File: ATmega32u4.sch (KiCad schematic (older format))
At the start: 36 parts, among them J1 USB_B_Mini, U4 ATmega32U4RC-MU, Y1 16MHz

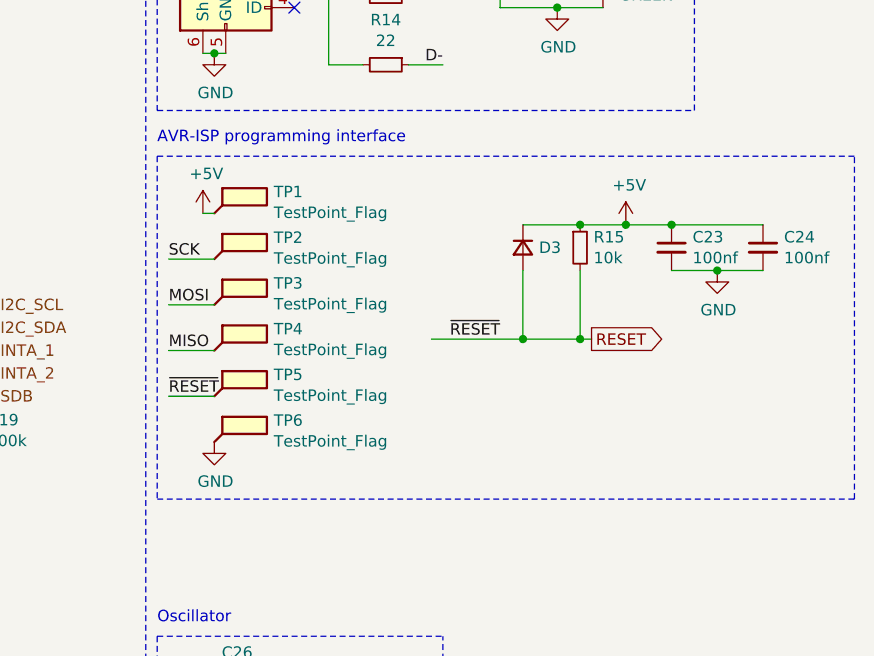
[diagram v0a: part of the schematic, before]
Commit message: Switch to jtag
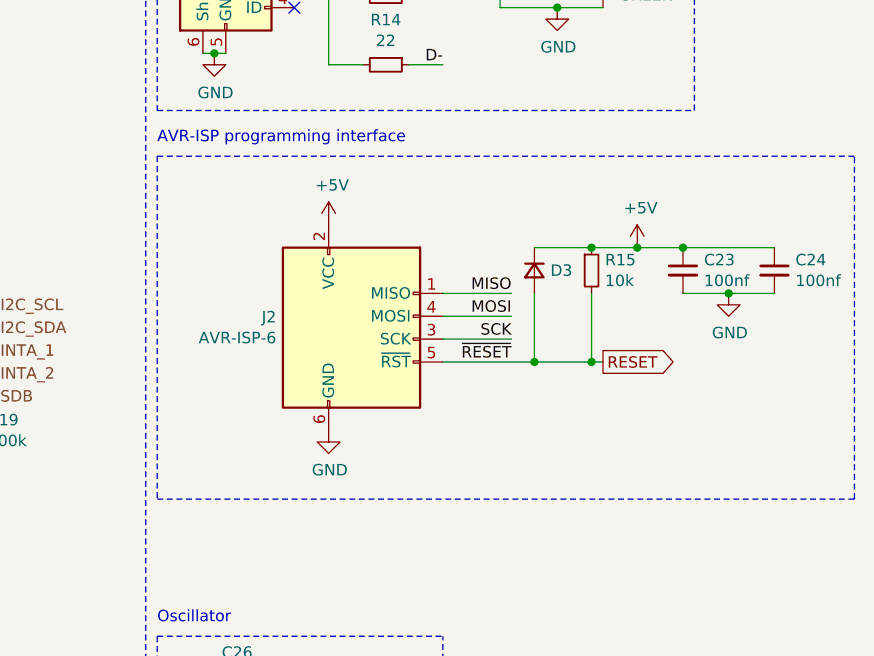
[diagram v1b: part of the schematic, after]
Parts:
- removed TP1, TP2, TP3, TP4, TP5, TP6: TestPoint_Flag, TestPoint:TestPoint_THTPad_D1.0mm_Drill0.5mm, symbol Connector:TestPoint_Flag
- added J2: AVR-ISP-6, Connector:Tag-Connect_TC2030-IDC-NL_2x03_P1.27mm_Vertical, symbol Connector:AVR-ISP-6
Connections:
- net +5V: now also J2.2 (VCC)
- net GND: now also J2.6 (GND)
- net MISO: now also J2.1 (MISO)
- net MOSI: now also J2.4 (MOSI)
- net RESET: now also J2.5 (~RST)
- net SCK: now also J2.3 (SCK)
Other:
- moved on the sheet: C23, C24, D3, R15

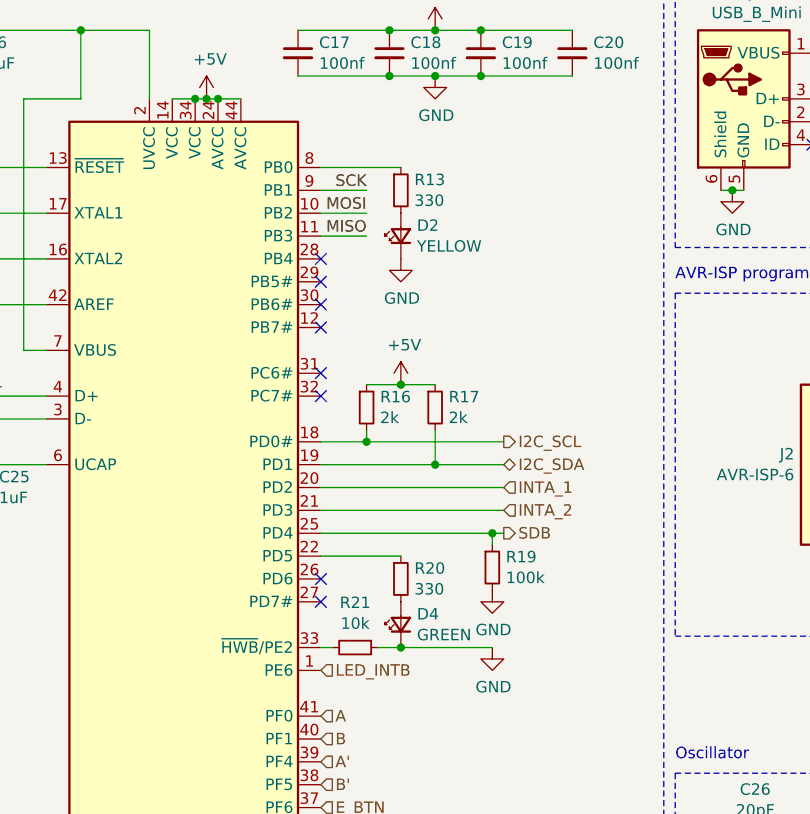
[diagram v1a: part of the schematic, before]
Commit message: ATmega32u4 layout in progress
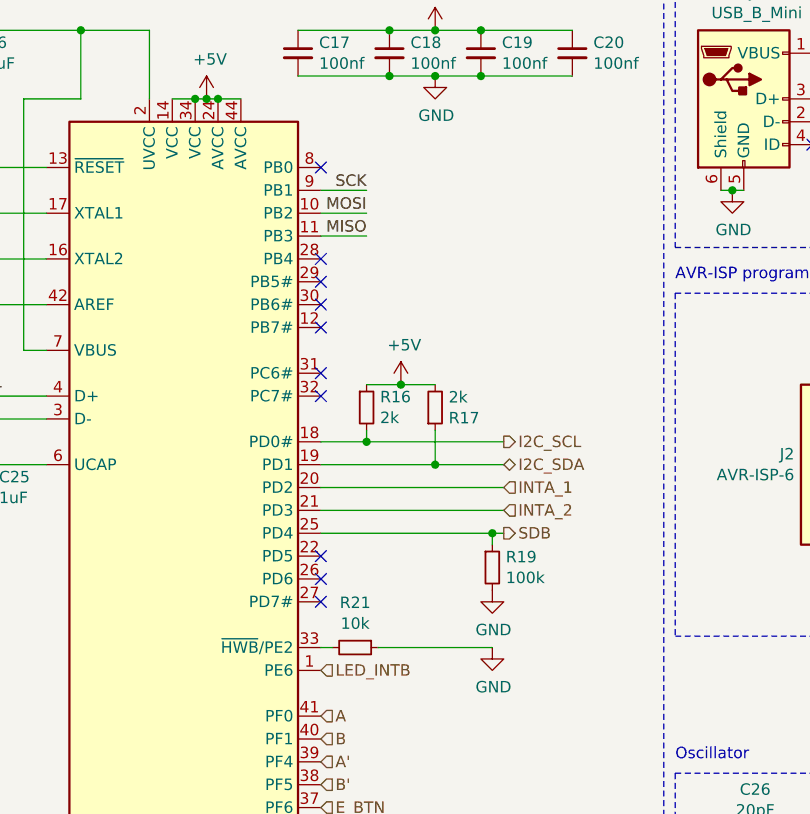
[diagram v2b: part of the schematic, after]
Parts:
- removed D2: YELLOW, Collins-FMS-3000:LED_0603_1608Metric, symbol Device:LED_Small
- removed D4: GREEN, Collins-FMS-3000:LED_0603_1608Metric, symbol Device:LED_Small
- removed R13, R20: 330, Collins-FMS-3000:Perfect_0402, symbol Device:R_Small
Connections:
- net +5V: now also R17.2; no longer R17.1
- net I2C_SDA: now also R17.1; no longer R17.2
- no-connect marks 10 -> 12
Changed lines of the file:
@@
-$EndComp
-$Comp
-L Device:R_Small R?
-U 1 1 61B111E6
-P 2750 1650
-AR Path="/61B111E6" Ref="R?"  Part="1"
-AR Path="/61F7F1B9/61B111E6" Ref="R?"  Part="1"
-AR Path="/61AFDA18/61B111E6" Ref="R13"  Part="1"
-F 0 "R13" H 2809 1696 50  0000 L CNN
-F 1 "330" H 2809 1605 50  0000 L CNN
-F 2 "Collins-FMS-3000:Perfect_0402" H 2750 1650 50  0001 C CNN
-F 3 "~" H 2750 1650 50  0001 C CNN
-F 4 "0402" H 2750 1650 50  0001 C CNN "JLC"
-F 5 "C25104" H 2750 1650 50  0001 C CNN "LCSC"
-	1    2750 1650
-	1    0    0    -1
-$EndComp
-$Comp
-L Device:LED_Small D?
-U 1 1 61B111EE
-P 2750 1850
-AR Path="/61B111EE" Ref="D?"  Part="1"
-AR Path="/61F7F1B9/61B111EE" Ref="D?"  Part="1"
-AR Path="/61AFDA18/61B111EE" Ref="D2"  Part="1"
-F 0 "D2" V 2796 1780 50  0000 R CNN
-F 1 "YELLOW" V 2705 1780 50  0000 R CNN
-F 2 "Collins-FMS-3000:LED_0603_1608Metric" V 2750 1850 50  0001 C CNN
-F 3 "~" V 2750 1850 50  0001 C CNN
-F 4 "0603" H 2750 1850 50  0001 C CNN "JLC"
-F 5 "C72038" H 2750 1850 50  0001 C CNN "LCSC"
-	1    2750 1850
-	0    -1   -1   0
-$EndComp
-$Comp
-L power:GND #PWR?
-U 1 1 61B111F4
-P 2750 1950
-AR Path="/61B111F4" Ref="#PWR?"  Part="1"
-AR Path="/61F7F1B9/61B111F4" Ref="#PWR?"  Part="1"
-AR Path="/61AFDA18/61B111F4" Ref="#PWR016"  Part="1"
-F 0 "#PWR016" H 2750 1700 50  0001 C CNN
-F 1 "GND" H 2755 1777 50  0000 C CNN
-F 2 "" H 2750 1950 50  0001 C CNN
-F 3 "" H 2750 1950 50  0001 C CNN
-	1    2750 1950
-	1    0    0    -1
-$EndComp
-$Comp
-L Device:R_Small R?
-U 1 1 61B111FC
-P 2750 3350
-AR Path="/61B111FC" Ref="R?"  Part="1"
-AR Path="/61F7F1B9/61B111FC" Ref="R?"  Part="1"
-AR Path="/61AFDA18/61B111FC" Ref="R20"  Part="1"
-F 0 "R20" H 2809 3396 50  0000 L CNN
-F 1 "330" H 2809 3305 50  0000 L CNN
-F 2 "Collins-FMS-3000:Perfect_0402" H 2750 3350 50  0001 C CNN
-F 3 "~" H 2750 3350 50  0001 C CNN
-F 4 "0402" H 2750 3350 50  0001 C CNN "JLC"
-F 5 "C25104" H 2750 3350 50  0001 C CNN "LCSC"
-	1    2750 3350
-	1    0    0    -1
-$EndComp
-$Comp
-L Device:LED_Small D?
-U 1 1 61B11203
-P 2750 3550
-AR Path="/61B11203" Ref="D?"  Part="1"
-AR Path="/61F7F1B9/61B11203" Ref="D?"  Part="1"
-AR Path="/61AFDA18/61B11203" Ref="D4"  Part="1"
-F 0 "D4" V 2796 3480 50  0000 R CNN
-F 1 "GREEN" V 2705 3480 50  0000 R CNN
-F 2 "Collins-FMS-3000:LED_0603_1608Metric" V 2750 3550 50  0001 C CNN
-F 3 "~" V 2750 3550 50  0001 C CNN
-F 4 "0603" H 2750 3550 50  0001 C CNN "JLC"
-	1    2750 3550
-	0    -1   -1   0
 $EndComp
 $Comp
@@
 Text Notes 3950 4150 0    50   ~ 0
 Oscillator
-Wire Wire Line
-	2400 1550 2750 1550
 Text Label 2600 1650 2    50   ~ 0
 SCK
@@
 Wire Wire Line
 	2400 3650 2450 3650
-Wire Wire Line
-	2650 3650 2750 3650
-Connection ~ 2750 3650
-Wire Wire Line
-	2400 3250 2750 3250
 Wire Notes Line
 	550  700  550  5100
@@
 F 5 "C17604" H 2900 2600 50  0001 C CNN "LCSC"
 	1    2900 2600
-	1    0    0    -1
+	1    0    0    1
 $EndComp
 Wire Wire Line
@@
 Text HLabel 3200 2950 2    50   Input ~ 0
 INTA_1
-Wire Wire Line
-	3150 3650 2750 3650
 Wire Wire Line
 	2400 2750 2600 2750
@@
 Text Label 5500 2900 2    50   ~ 0
 SCK
+Wire Wire Line
+	2650 3650 3150 3650
+NoConn ~ 2400 3250
+NoConn ~ 2400 1550
 $EndSCHEMATC

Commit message: More routing. What a pain.
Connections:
- net +5V: no longer U4.44 (AVCC)
- net A: now also U4.28 (PB4); no longer U4.41 (PF0)
- net A': now also U4.29 (PB5#); no longer U4.39 (PF4)
- net B: now also U4.30 (PB6#); no longer U4.40 (PF1)
- net B': now also U4.31 (PC6#); no longer U4.38 (PF5)
- net INTA_2: now also U4.1 (PE6); no longer U4.21 (PD3)
- net LED_INTB: now also U4.21 (PD3); no longer U4.1 (PE6)
- net SDB: now also U4.27 (PD7#); no longer U4.25 (PD4)
- net E_BTN: no longer names the net of U4.37 (PF6)
- no-connect marks 12 -> 13
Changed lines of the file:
@@
 Wire Wire Line
 	1750 4850 1800 4850
-NoConn ~ 2400 1950
-NoConn ~ 2400 2050
-NoConn ~ 2400 2150
 NoConn ~ 2400 2250
-NoConn ~ 2400 2450
-NoConn ~ 2400 2550
 NoConn ~ 2400 3350
-NoConn ~ 2400 3450
 NoConn ~ 2400 4450
 $Comp
@@
 Wire Wire Line
 	2750 2500 2900 2500
-Text HLabel 2400 3750 2    50   Input ~ 0
+Text HLabel 3200 3050 2    50   Input ~ 0
 LED_INTB
 Text HLabel 3200 2950 2    50   Input ~ 0
@@
 	3200 2950 2400 2950
 Wire Wire Line
-	2400 3150 3150 3150
-Wire Wire Line
 	3200 3150 3150 3150
-Connection ~ 3150 3150
 Wire Wire Line
 	2400 3050 3200 3050
-Text HLabel 3200 3050 2    50   Input ~ 0
+Text HLabel 2400 3750 2    50   Input ~ 0
 INTA_2
 Wire Wire Line
 	950  1550 1200 1550
-Text HLabel 2400 3950 2    50   Input ~ 0
+Text HLabel 3100 1800 2    50   Input ~ 0
 A
-Text HLabel 2400 4050 2    50   Input ~ 0
+Text HLabel 3100 1900 2    50   Input ~ 0
+A'
+Text HLabel 3100 2000 2    50   Input ~ 0
 B
-Text HLabel 2400 4150 2    50   Input ~ 0
-A'
-Text HLabel 2400 4250 2    50   Input ~ 0
+Text HLabel 3100 2100 2    50   Input ~ 0
 B'
-Text HLabel 2400 4350 2    50   Input ~ 0
-E_BTN
 $Comp
 L CJ4-MFD-Menu-Panel:ATmega32U4RC-MU U4
@@
 	1    0    0    -1
 $EndComp
-Wire Wire Line
-	1900 1250 1950 1250
-Wire Wire Line
-	1850 1250 1900 1250
 Connection ~ 5600 3000
-Wire Wire Line
-	1750 1250 1850 1250
-Connection ~ 1850 1250
-Connection ~ 1950 1250
-Wire Wire Line
-	1950 1250 2050 1250
 Wire Notes Line
 	3950 3600 7000 3600
@@
 	5200 2900 5500 2900
 $Comp
-L power:+5V #PWR?
+L power:+5V #PWR0115
 U 1 1 61AC5B6E
 P 4700 2400
-F 0 "#PWR?" H 4700 2250 50  0001 C CNN
+F 0 "#PWR0115" H 4700 2250 50  0001 C CNN
 F 1 "+5V" H 4715 2573 50  0000 C CNN
 F 2 "" H 4700 2400 50  0001 C CNN
@@
 $EndComp
 $Comp
-L power:GND #PWR?
+L power:GND #PWR0124
 U 1 1 61AC65BA
 P 4700 3300
-F 0 "#PWR?" H 4700 3050 50  0001 C CNN
+F 0 "#PWR0124" H 4700 3050 50  0001 C CNN
 F 1 "GND" H 4705 3127 50  0000 C CNN
 F 2 "" H 4700 3300 50  0001 C CNN
@@
 NoConn ~ 2400 3250
 NoConn ~ 2400 1550
+Wire Wire Line
+	1900 1250 1950 1250
+Connection ~ 1850 1250
+Wire Wire Line
+	1850 1250 1900 1250
+Wire Wire Line
+	1750 1250 1850 1250
+Wire Wire Line
+	2400 2450 2500 2450
+Wire Wire Line
+	2500 2450 2500 2400
+Wire Wire Line
+	2500 2400 2600 2400
+Wire Wire Line
+	2600 2400 2600 2100
+Wire Wire Line
+	2600 2100 3100 2100
+Wire Wire Line
+	2400 2150 2550 2150
+Wire Wire Line
+	2550 2150 2550 2000
+Wire Wire Line
+	2550 2000 3100 2000
+Wire Wire Line
+	2400 2050 2500 2050
+Wire Wire Line
+	2500 2050 2500 1900
+Wire Wire Line
+	2500 1900 3100 1900
+Wire Wire Line
+	2400 1950 2950 1950
+Wire Wire Line
+	2950 1950 2950 1800
+Wire Wire Line
+	2950 1800 3100 1800
+NoConn ~ 2400 3950
+NoConn ~ 2400 4050
+NoConn ~ 2400 4150
+NoConn ~ 2400 4250
+NoConn ~ 2400 4350
+Wire Wire Line
+	2400 3450 2450 3450
+Wire Wire Line
+	2450 3450 2450 3150
+Wire Wire Line
+	2450 3150 3150 3150
+Connection ~ 3150 3150
+NoConn ~ 2400 3150
+NoConn ~ 2400 2550
 $EndSCHEMATC

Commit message: Partiall routed but going to rip it all up and start over
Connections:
- net +5V: now also U4.44 (AVCC)
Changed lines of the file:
@@
 NoConn ~ 2400 3150
 NoConn ~ 2400 2550
+Wire Wire Line
+	1950 1250 2050 1250
+Connection ~ 1950 1250
 $EndSCHEMATC

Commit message: Fully routed and ready to go
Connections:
- net B: now also U4.31 (PC6#); no longer U4.30 (PB6#)
- net B': now also U4.30 (PB6#); no longer U4.31 (PC6#)
- net CTR: now reaches U4.36 (PF7)
- net UP: now reaches U4.37 (PF6)
- net RIGHT: now reaches U4.38 (PF5)
- net DOWN: now reaches U4.39 (PF4)
- net LEFT: now reaches U4.40 (PF1)
- no-connect marks 13 -> 8
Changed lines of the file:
@@
 NoConn ~ 2400 2250
 NoConn ~ 2400 3350
-NoConn ~ 2400 4450
 $Comp
 L Device:C_Small C?
@@
 A'
 Text HLabel 3100 2000 2    50   Input ~ 0
+B'
+Text HLabel 3100 2100 2    50   Input ~ 0
 B
-Text HLabel 3100 2100 2    50   Input ~ 0
-B'
+Connection ~ 5600 3000
+Wire Notes Line
+	3950 3600 7000 3600
+Wire Notes Line
+	7000 3600 7000 2100
+Wire Notes Line
+	3950 2100 7000 2100
+Wire Notes Line
+	3950 2100 3950 3600
+$Comp
+L Connector:AVR-ISP-6 J2
+U 1 1 61AB060D
+P 4800 2900
+F 0 "J2" H 4471 2996 50  0000 R CNN
+F 1 "AVR-ISP-6" H 4471 2905 50  0000 R CNN
+F 2 "Connector:Tag-Connect_TC2030-IDC-NL_2x03_P1.27mm_Vertical" V 4550 2950 50  0001 C CNN
+F 3 " ~" H 3525 2350 50  0001 C CNN
+	1    4800 2900
+	1    0    0    -1
+$EndComp
+Wire Wire Line
+	5200 2700 5500 2700
+Wire Wire Line
+	5200 2800 5500 2800
+Wire Wire Line
+	5200 2900 5500 2900
+$Comp
+L power:+5V #PWR0115
+U 1 1 61AC5B6E
+P 4700 2400
+F 0 "#PWR0115" H 4700 2250 50  0001 C CNN
+F 1 "+5V" H 4715 2573 50  0000 C CNN
+F 2 "" H 4700 2400 50  0001 C CNN
+F 3 "" H 4700 2400 50  0001 C CNN
+	1    4700 2400
+	1    0    0    -1
+$EndComp
+$Comp
+L power:GND #PWR0124
+U 1 1 61AC65BA
+P 4700 3300
+F 0 "#PWR0124" H 4700 3050 50  0001 C CNN
+F 1 "GND" H 4705 3127 50  0000 C CNN
+F 2 "" H 4700 3300 50  0001 C CNN
+F 3 "" H 4700 3300 50  0001 C CNN
+	1    4700 3300
+	1    0    0    -1
+$EndComp
+Text Label 5500 2700 2    50   ~ 0
+MISO
+Text Label 5500 2800 2    50   ~ 0
+MOSI
+Text Label 5500 2900 2    50   ~ 0
+SCK
+Wire Wire Line
+	2650 3650 3150 3650
+NoConn ~ 2400 3250
+NoConn ~ 2400 1550
+Wire Wire Line
+	2400 2450 2500 2450
+Wire Wire Line
+	2500 2450 2500 2400
+Wire Wire Line
+	2500 2400 2600 2400
+Wire Wire Line
+	2600 2400 2600 2100
+Wire Wire Line
+	2600 2100 3100 2100
+Wire Wire Line
+	2400 2150 2550 2150
+Wire Wire Line
+	2550 2150 2550 2000
+Wire Wire Line
+	2550 2000 3100 2000
+Wire Wire Line
+	2400 2050 2500 2050
+Wire Wire Line
+	2500 2050 2500 1900
+Wire Wire Line
+	2500 1900 3100 1900
+Wire Wire Line
+	2400 1950 2950 1950
+Wire Wire Line
+	2950 1950 2950 1800
+Wire Wire Line
+	2950 1800 3100 1800
+NoConn ~ 2400 3950
+Wire Wire Line
+	2400 3450 2450 3450
+Wire Wire Line
+	2450 3450 2450 3150
+Wire Wire Line
+	2450 3150 3150 3150
+Connection ~ 3150 3150
+NoConn ~ 2400 3150
+NoConn ~ 2400 2550
+Wire Wire Line
+	1750 1250 1850 1250
+Wire Wire Line
+	1850 1250 1900 1250
+Connection ~ 1850 1250
+Wire Wire Line
+	1950 1250 2050 1250
+Wire Wire Line
+	1900 1250 1950 1250
+Connection ~ 1950 1250
 $Comp
 L CJ4-MFD-Menu-Panel:ATmega32U4RC-MU U4
@@
 	1    0    0    -1
 $EndComp
-Connection ~ 5600 3000
-Wire Notes Line
-	3950 3600 7000 3600
-Wire Notes Line
-	7000 3600 7000 2100
-Wire Notes Line
-	3950 2100 7000 2100
-Wire Notes Line
-	3950 2100 3950 3600
-$Comp
-L Connector:AVR-ISP-6 J2
-U 1 1 61AB060D
-P 4800 2900
-F 0 "J2" H 4471 2996 50  0000 R CNN
-F 1 "AVR-ISP-6" H 4471 2905 50  0000 R CNN
-F 2 "Connector:Tag-Connect_TC2030-IDC-NL_2x03_P1.27mm_Vertical" V 4550 2950 50  0001 C CNN
-F 3 " ~" H 3525 2350 50  0001 C CNN
-	1    4800 2900
-	1    0    0    -1
-$EndComp
-Wire Wire Line
-	5200 2700 5500 2700
-Wire Wire Line
-	5200 2800 5500 2800
-Wire Wire Line
-	5200 2900 5500 2900
-$Comp
-L power:+5V #PWR0115
-U 1 1 61AC5B6E
-P 4700 2400
-F 0 "#PWR0115" H 4700 2250 50  0001 C CNN
-F 1 "+5V" H 4715 2573 50  0000 C CNN
-F 2 "" H 4700 2400 50  0001 C CNN
-F 3 "" H 4700 2400 50  0001 C CNN
-	1    4700 2400
-	1    0    0    -1
-$EndComp
-$Comp
-L power:GND #PWR0124
-U 1 1 61AC65BA
-P 4700 3300
-F 0 "#PWR0124" H 4700 3050 50  0001 C CNN
-F 1 "GND" H 4705 3127 50  0000 C CNN
-F 2 "" H 4700 3300 50  0001 C CNN
-F 3 "" H 4700 3300 50  0001 C CNN
-	1    4700 3300
-	1    0    0    -1
-$EndComp
-Text Label 5500 2700 2    50   ~ 0
-MISO
-Text Label 5500 2800 2    50   ~ 0
-MOSI
-Text Label 5500 2900 2    50   ~ 0
-SCK
-Wire Wire Line
-	2650 3650 3150 3650
-NoConn ~ 2400 3250
-NoConn ~ 2400 1550
-Wire Wire Line
-	1900 1250 1950 1250
-Connection ~ 1850 1250
-Wire Wire Line
-	1850 1250 1900 1250
-Wire Wire Line
-	1750 1250 1850 1250
-Wire Wire Line
-	2400 2450 2500 2450
-Wire Wire Line
-	2500 2450 2500 2400
-Wire Wire Line
-	2500 2400 2600 2400
-Wire Wire Line
-	2600 2400 2600 2100
-Wire Wire Line
-	2600 2100 3100 2100
-Wire Wire Line
-	2400 2150 2550 2150
-Wire Wire Line
-	2550 2150 2550 2000
-Wire Wire Line
-	2550 2000 3100 2000
-Wire Wire Line
-	2400 2050 2500 2050
-Wire Wire Line
-	2500 2050 2500 1900
-Wire Wire Line
-	2500 1900 3100 1900
-Wire Wire Line
-	2400 1950 2950 1950
-Wire Wire Line
-	2950 1950 2950 1800
-Wire Wire Line
-	2950 1800 3100 1800
-NoConn ~ 2400 3950
-NoConn ~ 2400 4050
-NoConn ~ 2400 4150
-NoConn ~ 2400 4250
-NoConn ~ 2400 4350
-Wire Wire Line
-	2400 3450 2450 3450
-Wire Wire Line
-	2450 3450 2450 3150
-Wire Wire Line
-	2450 3150 3150 3150
-Connection ~ 3150 3150
-NoConn ~ 2400 3150
-NoConn ~ 2400 2550
-Wire Wire Line
-	1950 1250 2050 1250
-Connection ~ 1950 1250
+Text HLabel 2400 4450 2    50   Input ~ 0
+CTR
+Text HLabel 2400 4350 2    50   Input ~ 0
+UP
+Text HLabel 2400 4250 2    50   Input ~ 0
+RIGHT
+Text HLabel 2400 4150 2    50   Input ~ 0
+DOWN
+Text HLabel 2400 4050 2    50   Input ~ 0
+LEFT
 $EndSCHEMATC
